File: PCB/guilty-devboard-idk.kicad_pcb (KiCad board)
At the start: 2 copper layers, 5 x 13.8 mm, 1 part

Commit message: commit idk pre-10.0 update
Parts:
- removed the REF** at (164.3, 116.7)
- added REF**: Nordic_FCCSP-98_3.67x3.85mm_Layout10x10_P0.35mm_Offcenter, PCM_nordic-lib-kicad-nrf54l:Nordic_FCCSP-98_3.67x3.85mm_Layout10x10_P0.35mm_Offcenter, F.Cu at (137.8, 90.9)
- added REF**: BGA-94_10x10_3.544x3.607mm, PCM_nordic-lib-kicad-nrf52:BGA-94_10x10_3.544x3.607mm, F.Cu at (126.2, 92.9)
- added REF**: SW_SPST_B3U-1000P, Button_Switch_SMD:SW_SPST_B3U-1000P, F.Cu at (131.4, 83.3)
- added REF**: Guilty Devboard Xrd pads, guilty-devboard-idk:Guilty Devboard Xrd pads, F.Cu at (109.0, 125.0)
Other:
- board outline removed

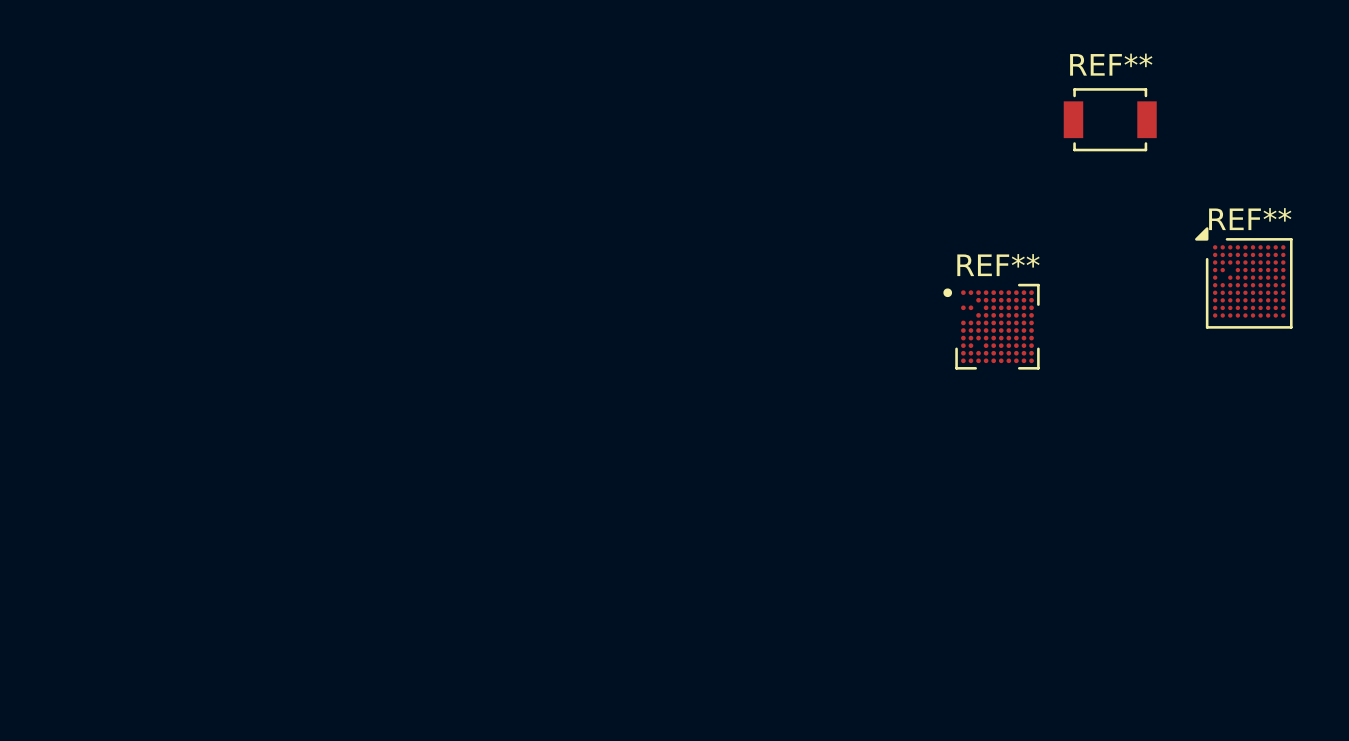
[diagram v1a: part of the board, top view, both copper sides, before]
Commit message: update idk schematic is done aside from switching out 3.3V
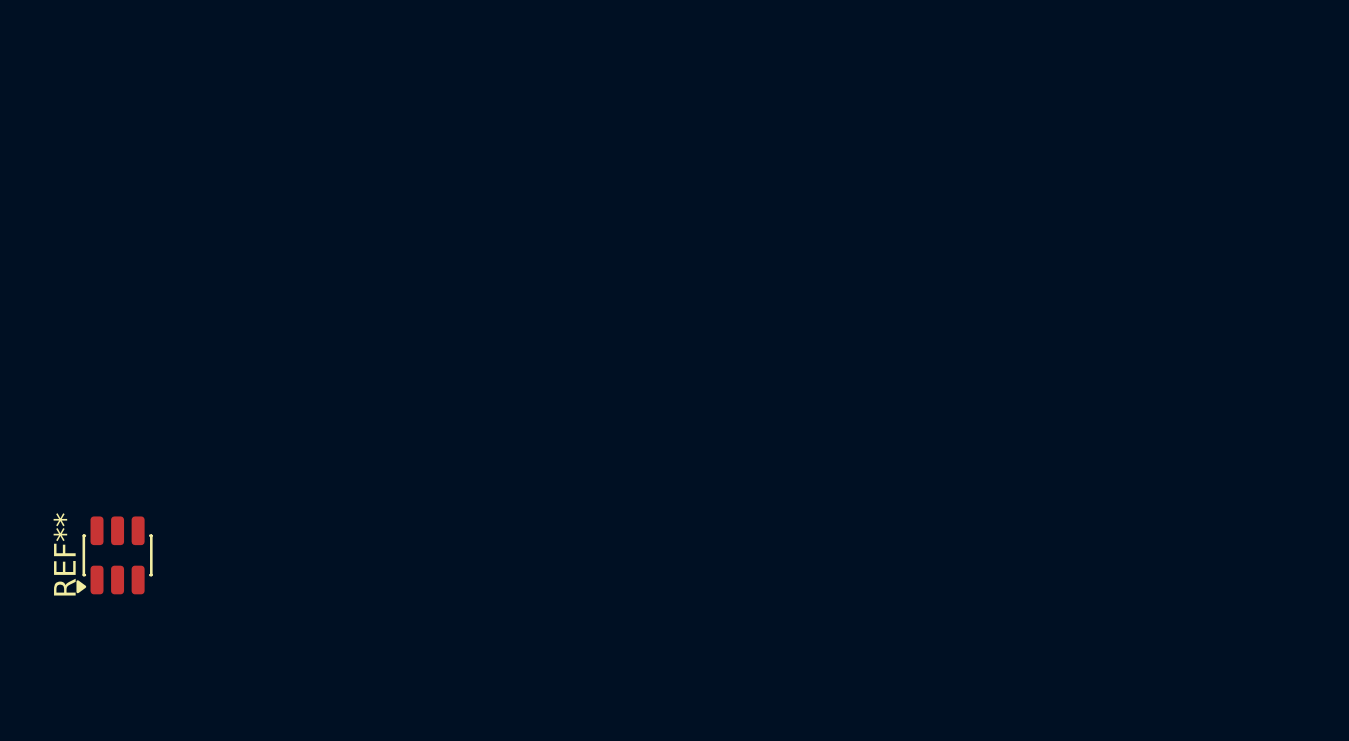
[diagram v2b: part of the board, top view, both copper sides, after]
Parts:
- removed the REF** at (137.8, 90.9)
- removed the REF** at (126.2, 92.9)
- removed the REF** at (131.4, 83.3)
- added REF**: SOT-23-6, Package_TO_SOT_SMD:SOT-23-6, F.Cu at (85.5, 103.4)

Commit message: terrible half done routing idk - post-decent filter routing
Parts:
- removed REF**: SOT-23-6, Package_TO_SOT_SMD:SOT-23-6
- removed REF**: Guilty Devboard Xrd pads, guilty-devboard-idk:Guilty Devboard Xrd pads
- added AE1: Antenna_Chip, PCM_marbastlib-various:2450AT18D0100001E_L, F.Cu at (120.0, 61.5)
- added C1: 10uF, Capacitor_SMD:C_0201_0603Metric, F.Cu at (63.2, 28.5)
- added C10: 4.7uF, Capacitor_SMD:C_0201_0603Metric, F.Cu at (108.7, 75.5)
- added C11: 4.7uF, Capacitor_SMD:C_0201_0603Metric, F.Cu at (66.0, 34.4)
- added C12: 0.1uF, Capacitor_SMD:C_0201_0603Metric, F.Cu at (117.0, 59.2)
- added C13: 2.2uF, Capacitor_SMD:C_0201_0603Metric, F.Cu at (45.5, 30.7)
- added C14: 4.7uF, Capacitor_SMD:C_0201_0603Metric, F.Cu at (68.9, 28.5)
- added C15: 1.5pF, Capacitor_SMD:C_0201_0603Metric, F.Cu at (118.7, 52.6)
- added C16: 22uF, Capacitor_SMD:C_0201_0603Metric, F.Cu at (115.2, 59.2)
- added C17: 4.7uF, Capacitor_SMD:C_0201_0603Metric, F.Cu at (113.8, 61.4)
- added C18: 1.2pF, Capacitor_SMD:C_0201_0603Metric, F.Cu at (118.7, 54.7)
- added C19: 22uF, Capacitor_SMD:C_0201_0603Metric, F.Cu at (48.3, 30.7)
- added C2: 100nF, Capacitor_SMD:C_0201_0603Metric, F.Cu at (63.2, 30.5)
- added C20: 22uF, Capacitor_SMD:C_0201_0603Metric, F.Cu at (71.8, 28.5)
- added C21: 100nF, Capacitor_SMD:C_0201_0603Metric, F.Cu at (107.7, 42.2)
- added C22: 1uF, Capacitor_SMD:C_0201_0603Metric, F.Cu at (114.4, 75.5)
- added C23: 0.47uF, Capacitor_SMD:C_0201_0603Metric, F.Cu at (61.1, 67.4)
- added C3: DNP, Capacitor_SMD:C_0201_0603Metric, F.Cu at (118.7, 50.5)
- added C4: 4.7uF, Capacitor_SMD:C_0201_0603Metric, F.Cu at (113.8, 62.1)
- added C5: 1.0pF, Capacitor_SMD:C_0201_0603Metric, F.Cu at (109.8, 54.7)
- added C6: 2.2uF, Capacitor_SMD:C_0201_0603Metric, F.Cu at (63.2, 36.4)
- added C7: DNP, Capacitor_SMD:C_0201_0603Metric, F.Cu at (108.8, 61.7)
- added C8: 100nF, Capacitor_SMD:C_0201_0603Metric, F.Cu at (66.0, 28.5)
- added C9: 100nF, Capacitor_SMD:C_0201_0603Metric, F.Cu at (66.0, 30.5)
- added D2: D, Diode_SMD:D_SOD-882, F.Cu at (74.6, 28.7)
- added D3: D, Diode_SMD:D_SOD-882, F.Cu at (74.6, 31.0)
- added D4: D, Diode_SMD:D_SOD-323, F.Cu at (140.3, 52.8)
- added D5: D, Diode_SMD:D_SOD-323, F.Cu at (140.4, 55.9)
- added D6: D, Diode_SMD:D_SOD-882, F.Cu at (67.4, 68.6)
- added D7: D, Diode_SMD:D_SOD-882, F.Cu at (74.6, 35.7)
- added FB1: FerriteBead, Inductor_SMD:L_0201_0603Metric, F.Cu at (111.9, 62.1)
- added J1: USB_C_Receptacle_USB2.0_16P, Connector_USB:USB_C_Receptacle_Amphenol_124019772112A, F.Cu at (115.6, 43.1)
- added JP2: Jumper_2_Bridged, Resistor_SMD:R_0201_0603Metric, F.Cu at (107.0, 42.2)
- added L1: 3.3nH, Inductor_SMD:L_0201_0603Metric, F.Cu at (118.3, 51.5)
- added L2: 2.2uH, Inductor_SMD:L_0201_0603Metric, F.Cu at (109.5, 81.2)
- added L3: 1.5uH, Inductor_SMD:L_0201_0603Metric, F.Cu at (68.0, 74.5)
- added L4: 4.7nH, Inductor_SMD:L_0201_0603Metric, F.Cu at (118.3, 53.6)
- added L5: 3.6nH, Inductor_SMD:L_0201_0603Metric, F.Cu at (118.3, 55.7)
- added L6: 4.7uH, Inductor_SMD:L_0201_0603Metric, F.Cu at (110.9, 61.7)
- added L7: 1.0nH, Inductor_SMD:L_0201_0603Metric, F.Cu at (111.6, 54.7)
- added Q1: SP2038CNQ, easyeda2kicad:PDFN-6_L2.0-W2.0-P0.65-BL-EP-1, F.Cu at (115.2, 51.3)
- added Q2: Q_PMOS, guilty-devboard-idk:Vishay_PowerPAK_SC70-6L_Single, F.Cu at (111.8, 77.2)
- added R1: 5.1k, Resistor_SMD:R_0201_0603Metric, F.Cu at (117.3, 48.3)
- added R12: 10k, Resistor_SMD:R_0201_0603Metric, F.Cu at (108.4, 42.2)
- added R13: 1M, Resistor_SMD:R_0201_0603Metric, F.Cu at (41.9, 49.6)
- added R14: 220k, Resistor_SMD:R_0201_0603Metric, F.Cu at (116.8, 62.2)
- added R15: 68k, Resistor_SMD:R_0201_0603Metric, F.Cu at (117.0, 61.4)
- added R16: 2.2, Resistor_SMD:R_0201_0603Metric, F.Cu at (115.2, 61.7)
- added R17: 200, Resistor_SMD:R_0201_0603Metric, F.Cu at (44.8, 45.6)
- added R18: 1M, Resistor_SMD:R_0201_0603Metric, F.Cu at (44.8, 47.6)
- added R2: 5.1k, Resistor_SMD:R_0201_0603Metric, F.Cu at (118.7, 48.3)
- added R3: 470k, Resistor_SMD:R_0201_0603Metric, F.Cu at (112.4, 61.4)
- added R4: 30, Resistor_SMD:R_0201_0603Metric, F.Cu at (109.8, 61.4)
- added R5: 30, Resistor_SMD:R_0201_0603Metric, F.Cu at (109.8, 62.1)
- added R6: 2k, Resistor_SMD:R_0201_0603Metric, F.Cu at (116.5, 54.1)
- added R7: 1k, Resistor_SMD:R_0201_0603Metric, F.Cu at (115.2, 60.1)
- added R8: 806k, Resistor_SMD:R_0201_0603Metric, F.Cu at (115.2, 61.0)
- added R9: 2M, Resistor_SMD:R_0201_0603Metric, F.Cu at (41.9, 45.6)
- added U1: nRF54LM20A-PAXX, PCM_nordic-lib-kicad-nrf54l:Nordic_FCCSP-98_3.67x3.85mm_Layout10x10_P0.35mm_Offcenter, F.Cu at (111.4, 58.1)
- added U2: SGM40567-4.2XG/TR, easyeda2kicad:WLCSP-6_L1.2-W0.9-R3-C2-P0.40-TL, F.Cu at (116.9, 60.3)
- added U3: Xiao nRF52840 Connectors, guilty-devboard-idk:Guilty Devboard Xrd pads, F.Cu at (115.6, 47.0)
- added U4: MIC2876-5.0YMT-TR, easyeda2kicad:UDFN-8_L2.0-W2.0-P0.50-BL-EP, F.Cu at (111.0, 71.0)
- added U5: FH9261-G3JH, Package_TO_SOT_SMD:SOT-23-6, F.Cu at (116.0, 56.6)
- added U6: BD83070GWL-E2, guilty-devboard-idk:BD83070GWL, F.Cu at (64.4, 69.8)
- added Y1: 32MHz, Crystal:Crystal_SMD_2016-4Pin_2.0x1.6mm, F.Cu at (110.3, 53.0)
- added Y2: 32.768kHz, Crystal:Crystal_SMD_2016-4Pin_2.0x1.6mm, F.Cu at (113.3, 53.0)
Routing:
- net GND: track 0.00 -> 35.1 mm, vias 0 -> 20
- net /USB_D-: track 0.00 -> 31.8 mm, vias 0 -> 4
- net VBUS: track 0.00 -> 27.4 mm, vias 0 -> 3
- net /USB_D+: track 0.00 -> 25.3 mm, vias 0 -> 3
- net /P1.03_A/D0: track 0.00 -> 20.4 mm, vias 0 -> 2
- net Net-(U1A-DECA): track 0.00 -> 16.3 mm, vias 0 -> 3
- net /P2.09_UARTE00.CTS: track 0.00 -> 15.2 mm, vias 0 -> 2
- net /P2.07_UARTE00.RXD: track 0.00 -> 14.1 mm, vias 0 -> 1
- net /P1.04_A/D1: track 0.00 -> 13.9 mm, vias 0 -> 2
- net Net-(AE1-FEED): track 0.00 -> 13.8 mm
- net /ANT: track 0.00 -> 11.9 mm
- net /RESET: track 0.00 -> 11.4 mm, vias 0 -> 2
- net /P2.10_UARTE00.RTS: track 0.00 -> 10.2 mm, vias 0 -> 2
- net /P1.01_NFC1: track 0.00 -> 9.78 mm, vias 0 -> 2
- net /P1.30_A/D4_I2C_SDA: track 0.00 -> 9.27 mm
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- added copper zone on In3.Cu, net -BATT
- added copper zone on In1.Cu, net GND
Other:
- copper layers 2 -> 6

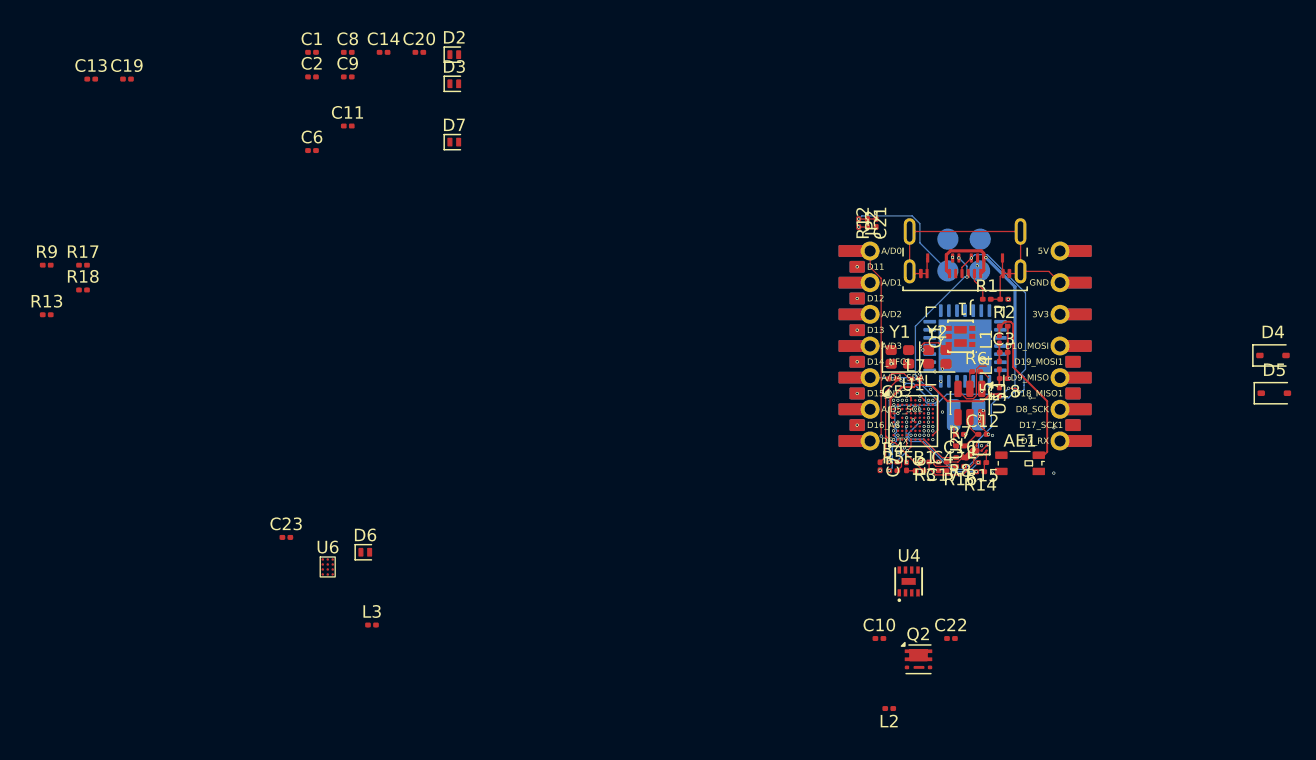
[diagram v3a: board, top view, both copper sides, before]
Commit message: fully routed
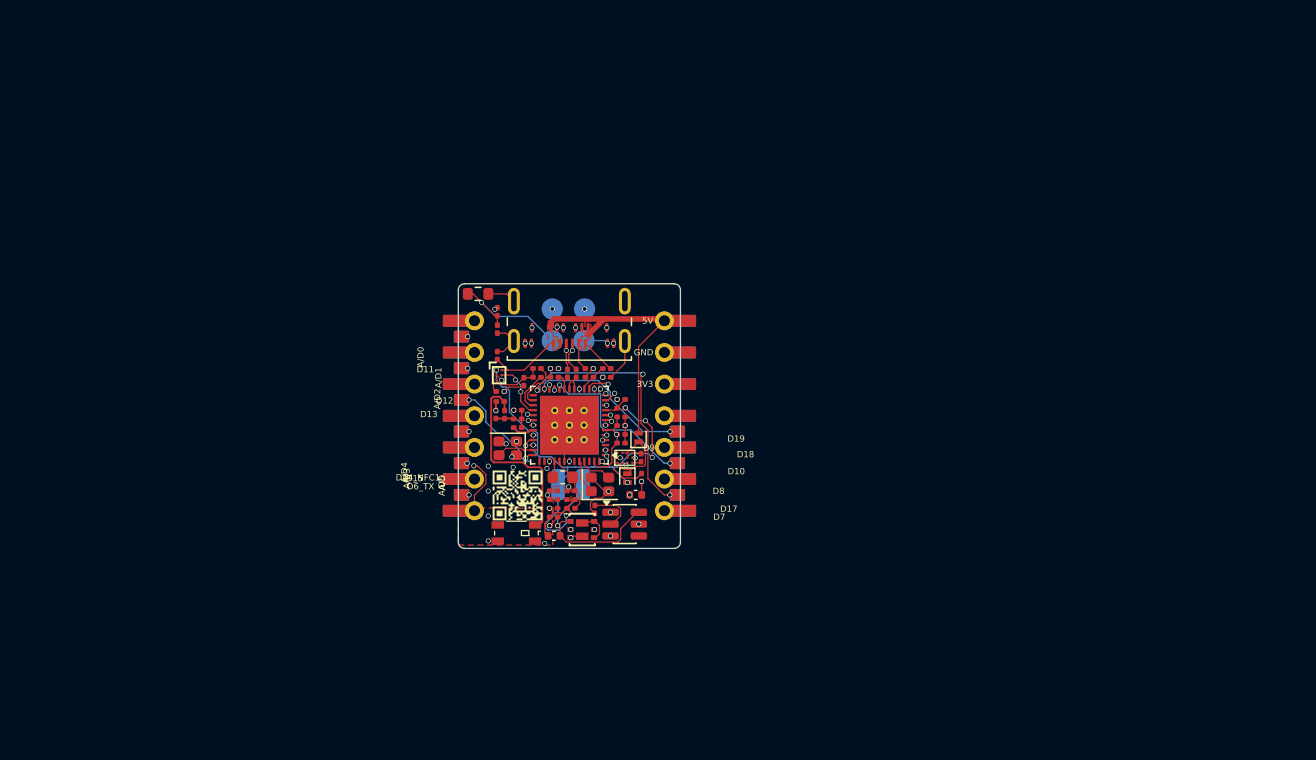
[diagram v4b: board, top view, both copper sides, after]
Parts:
- removed C10: 4.7uF, Capacitor_SMD:C_0201_0603Metric
- removed C20: 22uF, Capacitor_SMD:C_0201_0603Metric
- removed C22: 1uF, Capacitor_SMD:C_0201_0603Metric
- removed D2, D3: D, Diode_SMD:D_SOD-882
- removed D4, D5: D, Diode_SMD:D_SOD-323
- removed JP2: Jumper_2_Bridged, Resistor_SMD:R_0201_0603Metric
- removed L2: 2.2uH, Inductor_SMD:L_0201_0603Metric
- removed Q2: Q_PMOS, guilty-devboard-idk:Vishay_PowerPAK_SC70-6L_Single
- removed R13, R18: 1M, Resistor_SMD:R_0201_0603Metric
- removed U4: MIC2876-5.0YMT-TR, easyeda2kicad:UDFN-8_L2.0-W2.0-P0.50-BL-EP
- added G***: LOGO, LOGO, F.Cu at (79.7, 64.1)
- added G***: LOGO, LOGO, B.Cu at (83.8, 56.4)
- added JP1: Jumper_2_Open, Resistor_SMD:R_0603_1608Metric, F.Cu at (76.5, 47.9)
- C16, C19: footprint Capacitor_SMD:C_0201_0603Metric -> Capacitor_SMD:C_0402_1005Metric
- L6: footprint Inductor_SMD:L_0201_0603Metric -> Inductor_SMD:L_0603_1608Metric
- U1: value nRF54LM20A-PAXX -> nRF54LM20A-QGAA; footprint PCM_nordic-lib-kicad-nrf54l:Nordic_FCCSP-98_3.67x3.85mm_Layout10x10_P0.35mm_Offcenter -> PCM_nordic-lib-kicad-nrf54l:QFN-52-1EP_6x6mm_P0.4mm_EP4.7x4.7mm_ThermalVias
- U3: footprint guilty-devboard-idk:Guilty Devboard Xrd pads -> guilty-devboard-idk:Xiao nRF52840 Plus pads
- moved C19 52.7 mm to (89.1, 64.0)
- moved C13 47.8 mm to (86.8, 54.6), turned to 180 degrees
- moved R9 47.3 mm to (88.0, 56.4), turned to 180 degrees
- moved C15 41.1 mm to (77.9, 57.6), turned to -90 degrees
- moved C3 40.8 mm to (78.3, 56.5), turned to 0 degrees
- moved AE1 40.8 mm to (79.6, 67.1)
- moved L1 40.2 mm to (78.6, 57.6)
- moved U2 39.2 mm to (78.2, 54.4), turned to 0 degrees
- moved C18 39.1 mm to (79.7, 57.2), turned to 0 degrees
- moved L4 38.9 mm to (79.7, 57.9), turned to 180 degrees
- moved C1 38.9 mm to (88.0, 58.5)
- moved R17 38.9 mm to (82.6, 54.6)
- moved L5 38.8 mm to (79.7, 58.6), turned to 0 degrees
- moved C8 38.3 mm to (88.0, 59.9)
- moved C2 36.9 mm to (88.0, 57.8)
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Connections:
- AE1 pad 2: unconnected-(AE1-PCB_Trace-Pad2) -> GND
- R4 pad 2: Net-(U1A-D+) -> /MCU_USB_D+
- R5 pad 2: Net-(U1A-D-) -> /MCU_USB_D-
- U3 pad 11: /P2.02_QSPI.D0-SPIM.MOSI/SDO -> /P2.02_SPIM.MOSI/SDO_UARTE00.TXD
- U3 pad 12: /P2.04_QSPI.D1-SPIM.MISO/SDI -> /P2.04_SPIM.MISO/SDI_UARTE00.CTS
- U3 pad 13: /P2.01_QSPI/SPIM.SCK -> /P2.01_SPIM.SCK
- U3 pad 14: /P2.07_UARTE00.RXD -> /P2.00_SPIM.DCX_UARTE00.RXD
- U3 pad 15: /P2.09_UARTE00.CTS -> /P2.05_SPIM.CSN_UARTE00.RTS
- U3 pad 16: /P2.10_UARTE00.RTS -> /P1.08_D12
- U3 pad 17: /P0.03_GRTC.PWM -> /P1.15_D13
- U3 pad 21: /P2.03_QSPI.D2 -> /P0.03_GRTC.PWM
- U3 pad 22: /P2.00_QSPI.D3_SPIM.DCX -> /P1.07_GRTC.CLKOUTFAST
- U3 pad 23: /P2.05_QSPI.CSN -> /P0.04_GRTC.CLKOUT32K
- U3 pad 7: /P2.08_UARTE00.TXD -> /P1.09_D6
- U3 pad 8: +5V -> VBUS
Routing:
- net +BATT: track 5.84 -> 41.4 mm, vias 1 -> 6
- net /USB_D-: track 31.8 -> 4.28 mm, vias 4 -> 2
- net /USB_D+: track 25.3 -> 4.61 mm, vias 3 -> 2
- net /P0.04_GRTC.CLKOUT32K: track 0.00 -> 20.4 mm, vias 0 -> 3
- net /P1.02_NFC2: track 2.19 -> 19.3 mm
- net /P2.05_SPIM.CSN_UARTE00.RTS: track 0.00 -> 16.5 mm, vias 0 -> 2
- net /SWDCLK: track 0.00 -> 15.5 mm, vias 0 -> 2
- net /P2.09_UARTE00.CTS: track 15.2 -> 0.00 mm, vias 2 -> 0
- net /P1.06_A/D3: track 0.00 -> 14.8 mm
- net /P1.09_D6: track 0.00 -> 14.3 mm, vias 0 -> 2
- net /P2.07_UARTE00.RXD: track 14.1 -> 0.00 mm, vias 1 -> 0
- net /P1.07_GRTC.CLKOUTFAST: track 0.00 -> 13.9 mm, vias 1 -> 2
- net Net-(U1A-DECA): track 16.3 -> 2.45 mm, vias 3 -> 2
- net /SWDIO: track 0.00 -> 13.7 mm, vias 1 -> 2
- net /P1.31_A/D5_I2C_SCL: track 2.30 -> 13.9 mm, vias 0 -> 1
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- added copper zone on In3.Cu, net +3V3
- added copper zone on F.Cu, net GND
- added copper zone on F.Cu, net Net-(U1A-DECA)
- added copper zone on F.Cu, net VBUS
- added copper zone on In2.Cu, net VBUS
- removed copper zone on In3.Cu, net -BATT
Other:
- board outline added: 17.8 x 21.2 mm
